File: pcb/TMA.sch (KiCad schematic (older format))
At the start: 23 parts, among them J1 Conn_01x02, J2 Conn_01x06, SW1 SW_SPDT, U1 BMP280, U2 BMI160, U3 ATtiny1614-SS, U4 MIC5504-3.3YM5

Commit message: Update schema to have Schottky connected and 3V3 up.
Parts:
- removed D2: D_Schottky, symbol Device:D_Schottky
- added D?: D_Schottky, symbol Device:D_Schottky
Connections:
- net +3V3: now also D?.1 (K)
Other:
- moved on the sheet: R4, R5, U3
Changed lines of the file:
@@
 L MCU_Microchip_ATtiny:ATtiny1614-SS U3
 U 1 1 6079184C
-P 4550 3200
-F 0 "U3" H 4700 3900 50  0000 C CNN
-F 1 "ATtiny1614-SS" H 4150 3900 50  0000 C CNN
-F 2 "Package_SO:SOIC-14_3.9x8.7mm_P1.27mm" H 4550 3200 50  0001 C CIN
-F 3 "http://ww1.microchip.com/downloads/en/DeviceDoc/ATtiny1614-data-sheet-40001995A.pdf" H 4550 3200 50  0001 C CNN
-	1    4550 3200
+P 4100 3050
+F 0 "U3" H 4250 3750 50  0000 C CNN
+F 1 "ATtiny1614-SS" H 3700 3750 50  0000 C CNN
+F 2 "Package_SO:SOIC-14_3.9x8.7mm_P1.27mm" H 4100 3050 50  0001 C CIN
+F 3 "http://ww1.microchip.com/downloads/en/DeviceDoc/ATtiny1614-data-sheet-40001995A.pdf" H 4100 3050 50  0001 C CNN
+	1    4100 3050
 	1    0    0    -1
 $EndComp
@@
 L power:+3.3V #PWR07
 U 1 1 60798522
-P 4550 2500
-F 0 "#PWR07" H 4550 2350 50  0001 C CNN
-F 1 "+3.3V" H 4565 2673 50  0000 C CNN
-F 2 "" H 4550 2500 50  0001 C CNN
-F 3 "" H 4550 2500 50  0001 C CNN
-	1    4550 2500
+P 4100 2350
+F 0 "#PWR07" H 4100 2200 50  0001 C CNN
+F 1 "+3.3V" H 4115 2523 50  0000 C CNN
+F 2 "" H 4100 2350 50  0001 C CNN
+F 3 "" H 4100 2350 50  0001 C CNN
+	1    4100 2350
 	1    0    0    -1
 $EndComp
@@
 L power:GND #PWR08
 U 1 1 60798916
-P 4550 3900
-F 0 "#PWR08" H 4550 3650 50  0001 C CNN
-F 1 "GND" H 4555 3727 50  0000 C CNN
-F 2 "" H 4550 3900 50  0001 C CNN
-F 3 "" H 4550 3900 50  0001 C CNN
-	1    4550 3900
-	1    0    0    -1
-$EndComp
-Text GLabel 5150 2800 2    50   Input ~ 0
+P 4100 3750
+F 0 "#PWR08" H 4100 3500 50  0001 C CNN
+F 1 "GND" H 4105 3577 50  0000 C CNN
+F 2 "" H 4100 3750 50  0001 C CNN
+F 3 "" H 4100 3750 50  0001 C CNN
+	1    4100 3750
+	1    0    0    -1
+$EndComp
+Text GLabel 4700 2650 2    50   Input ~ 0
 UPDI
 $Comp
@@
 Wire Wire Line
 	7150 1150 7800 1150
-Wire Wire Line
-	7800 1050 7900 1050
 Connection ~ 7800 1050
-$Comp
-L Device:D_Schottky D2
-U 1 1 607CBF31
-P 7900 900
-F 0 "D2" V 7800 1050 50  0000 C CNN
-F 1 "D_Schottky" V 7900 1200 50  0000 C CNN
-F 2 "" H 7900 900 50  0001 C CNN
-F 3 "~" H 7900 900 50  0001 C CNN
-	1    7900 900
-	0    1    1    0
-$EndComp
-Wire Wire Line
-	7900 1050 8000 1050
-Connection ~ 7900 1050
 Text GLabel 8000 1050 2    50   Input ~ 0
 UPDI
@@
 Wire Notes Line
 	8450 500  8450 1850
-Wire Notes Line
-	500  4650 6750 4650
-Wire Notes Line
-	6750 500  6750 4650
-Wire Notes Line
-	500  4700 6800 4700
-Wire Notes Line
-	6800 4700 6800 1900
-Wire Notes Line
-	6800 1900 11200 1900
-Wire Notes Line
-	500  4750 6850 4750
-Wire Notes Line
-	6850 4750 6850 1950
-Wire Notes Line
-	6850 1950 11200 1950
-Text GLabel 5150 2900 2    50   Input ~ 0
+Text GLabel 4700 2750 2    50   Input ~ 0
 SDA
-Text GLabel 5150 3000 2    50   Input ~ 0
+Text GLabel 4700 2850 2    50   Input ~ 0
 SCL
 $Comp
@@
 Text GLabel 7150 1450 2    50   Input ~ 0
 SCL
-NoConn ~ 5150 3100
-NoConn ~ 5150 3200
-NoConn ~ 5150 3300
-NoConn ~ 5150 3400
-NoConn ~ 5150 3500
+NoConn ~ 4700 2950
+NoConn ~ 4700 3050
+NoConn ~ 4700 3150
+NoConn ~ 4700 3250
+NoConn ~ 4700 3350
 $Comp
 L Device:LED_Small D3
@@
 Text Notes 8900 600  2    50   ~ 0
 Indicators
-Text GLabel 3950 2800 0    50   Input ~ 0
+Text GLabel 3500 2650 0    50   Input ~ 0
 LED0
-Text GLabel 3950 2900 0    50   Input ~ 0
+Text GLabel 3500 2750 0    50   Input ~ 0
 LED1
-NoConn ~ 3950 3000
+NoConn ~ 3500 2850
 Text GLabel 8650 1000 1    50   Input ~ 0
 LED0
@@
 Wire Notes Line
 	9850 1850 9850 500
-Text GLabel 10300 850  1    50   Input ~ 0
+Text GLabel 10400 1000 0    50   Input ~ 0
 SCL
 $Comp
 L Device:R_Small R4
 U 1 1 60781223
-P 10300 950
-F 0 "R4" H 10150 900 50  0000 C CNN
-F 1 "10k" H 10150 1000 50  0000 C CNN
-F 2 "" H 10300 950 50  0001 C CNN
-F 3 "~" H 10300 950 50  0001 C CNN
-	1    10300 950
-	-1   0    0    1
+P 10500 1000
+F 0 "R4" V 10400 900 50  0000 C CNN
+F 1 "10k" V 10400 1050 50  0000 C CNN
+F 2 "" H 10500 1000 50  0001 C CNN
+F 3 "~" H 10500 1000 50  0001 C CNN
+	1    10500 1000
+	0    1    1    0
 $EndComp
 $Comp
 L Device:R_Small R5
 U 1 1 60781CEA
-P 10650 950
-F 0 "R5" H 10500 900 50  0000 C CNN
-F 1 "10k" H 10500 1000 50  0000 C CNN
-F 2 "" H 10650 950 50  0001 C CNN
-F 3 "~" H 10650 950 50  0001 C CNN
-	1    10650 950
-	-1   0    0    1
-$EndComp
-Text GLabel 10650 850  1    50   Input ~ 0
+P 10500 800
+F 0 "R5" V 10400 700 50  0000 C CNN
+F 1 "10k" V 10400 850 50  0000 C CNN
+F 2 "" H 10500 800 50  0001 C CNN
+F 3 "~" H 10500 800 50  0001 C CNN
+	1    10500 800
+	0    1    1    0
+$EndComp
+Text GLabel 10400 800  0    50   Input ~ 0
 SDA
 $Comp
 L power:+3.3V #PWR017
 U 1 1 60782162
-P 10650 1150
-F 0 "#PWR017" H 10650 1000 50  0001 C CNN
-F 1 "+3.3V" V 10650 1400 50  0000 C CNN
-F 2 "" H 10650 1150 50  0001 C CNN
-F 3 "" H 10650 1150 50  0001 C CNN
-	1    10650 1150
-	0    1    1    0
-$EndComp
-Wire Wire Line
-	10300 1050 10300 1100
-Wire Wire Line
-	10300 1100 10650 1100
-Wire Wire Line
-	10650 1100 10650 1150
-Wire Wire Line
-	10650 1050 10650 1100
-Connection ~ 10650 1100
+P 10700 800
+F 0 "#PWR017" H 10700 650 50  0001 C CNN
+F 1 "+3.3V" H 10850 900 50  0000 C CNN
+F 2 "" H 10700 800 50  0001 C CNN
+F 3 "" H 10700 800 50  0001 C CNN
+	1    10700 800
+	1    0    0    -1
+$EndComp
 Text Notes 9900 600  0    50   ~ 0
 I2C Pullups\n
@@
 Text Notes 9900 1300 0    50   ~ 0
 Mode Selector
-Text GLabel 3950 3100 0    50   Input ~ 0
+Text GLabel 3500 2950 0    50   Input ~ 0
 MODE
+Wire Wire Line
+	7800 1050 8000 1050
+Wire Wire Line
+	10600 800  10700 800
+Wire Wire Line
+	10700 1000 10700 800
+Wire Wire Line
+	10600 1000 10700 1000
+Connection ~ 10700 800
+$Comp
+L power:+3.3V #PWR?
+U 1 1 607905AF
+P 7900 700
+F 0 "#PWR?" H 7900 550 50  0001 C CNN
+F 1 "+3.3V" H 8100 800 50  0000 C CNN
+F 2 "" H 7900 700 50  0001 C CNN
+F 3 "" H 7900 700 50  0001 C CNN
+	1    7900 700
+	1    0    0    -1
+$EndComp
+$Comp
+L Device:D_Schottky D?
+U 1 1 607905B5
+P 7900 900
+F 0 "D?" V 7800 1050 50  0000 C CNN
+F 1 "D_Schottky" V 7900 1200 50  0000 C CNN
+F 2 "" H 7900 900 50  0001 C CNN
+F 3 "~" H 7900 900 50  0001 C CNN
+	1    7900 900
+	0    1    1    0
+$EndComp
+Wire Wire Line
+	7900 750  7900 700
+Wire Notes Line
+	5400 4650 5400 1850
+Wire Notes Line
+	500  4650 5400 4650
+Wire Notes Line
+	6750 1800 6750 500
 $EndSCHEMATC

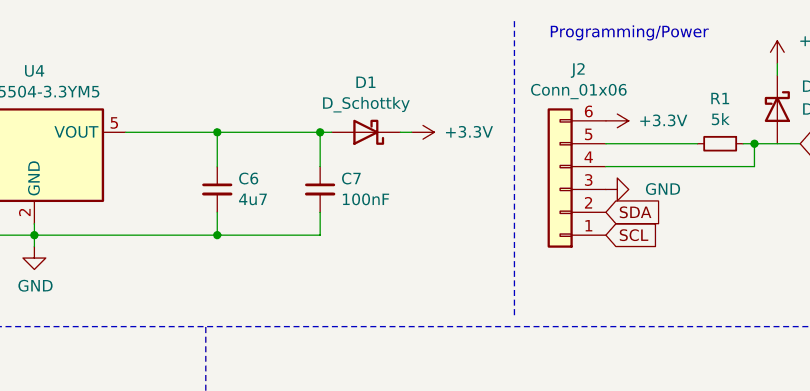
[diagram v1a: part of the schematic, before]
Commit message: Remove other Schottky.
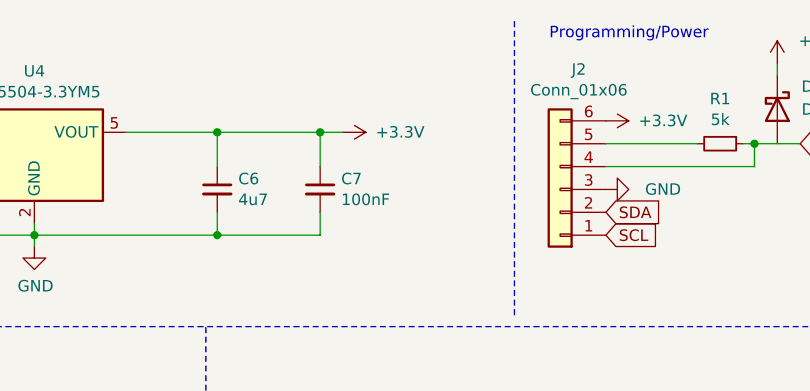
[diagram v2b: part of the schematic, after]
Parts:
- removed D1: D_Schottky, symbol Device:D_Schottky
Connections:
- net +3V3: now also C6.1, C7.1, U4.5 (VOUT)
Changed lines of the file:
@@
 L power:+3.3V #PWR010
 U 1 1 607B44BA
-P 6300 1000
-F 0 "#PWR010" H 6300 850 50  0001 C CNN
-F 1 "+3.3V" V 6300 1250 50  0000 C CNN
-F 2 "" H 6300 1000 50  0001 C CNN
-F 3 "" H 6300 1000 50  0001 C CNN
-	1    6300 1000
-	0    1    1    0
-$EndComp
-$Comp
-L Device:D_Schottky D1
-U 1 1 607B6FAB
-P 6100 1000
-F 0 "D1" H 6100 783 50  0000 C CNN
-F 1 "D_Schottky" H 6100 874 50  0000 C CNN
-F 2 "" H 6100 1000 50  0001 C CNN
-F 3 "~" H 6100 1000 50  0001 C CNN
-	1    6100 1000
-	-1   0    0    1
-$EndComp
-Wire Wire Line
-	5900 1000 5950 1000
+P 6000 1000
+F 0 "#PWR010" H 6000 850 50  0001 C CNN
+F 1 "+3.3V" V 6000 1250 50  0000 C CNN
+F 2 "" H 6000 1000 50  0001 C CNN
+F 3 "" H 6000 1000 50  0001 C CNN
+	1    6000 1000
+	0    1    1    0
+$EndComp
 Connection ~ 5900 1000
-Wire Wire Line
-	6250 1000 6300 1000
 $Comp
 L power:+3.3V #PWR011
@@
 Wire Notes Line
 	6750 1800 6750 500
+Wire Wire Line
+	5900 1000 6000 1000
 $EndSCHEMATC
